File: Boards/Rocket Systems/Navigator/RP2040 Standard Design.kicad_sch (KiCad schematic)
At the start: 41 parts, among them J5 DX07S016JA1R1500, J6 BM03B-SRSS-TBLFSN, U7 W25Q128JVSIQ TR, U8 ST1L05APU33R

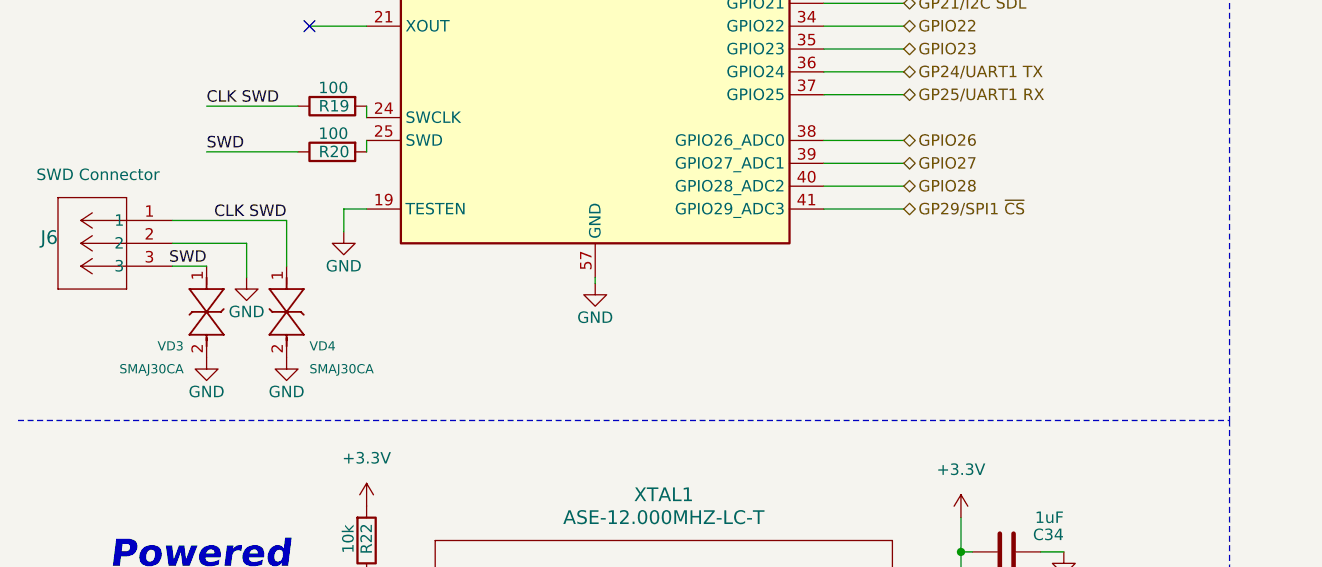
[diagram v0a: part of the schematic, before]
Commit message: ESD diodes and pinout update
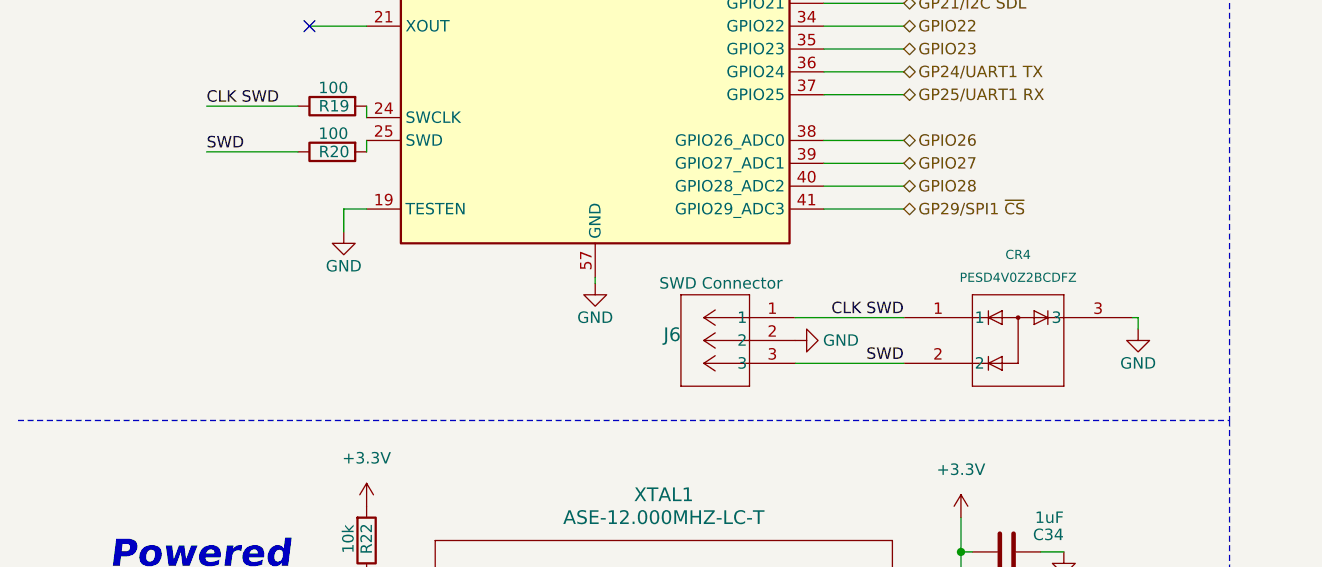
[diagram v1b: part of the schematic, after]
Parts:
- removed VD3, VD4: SMAJ30CA, SMAJ30CA:SMASeries_LTF, symbol SMAJ30CA:SMAJ30CA
- added CR4: PESD4V0Z2BCDFZ, DFN06033_SOT8013_NEX, symbol PESD4V0Z2BCDFZ:PESD4V0Z2BCDFZ
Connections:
- net CLK SWD: now also CR4.1
- net GND: now also CR4.3
- net SWD: now also CR4.2

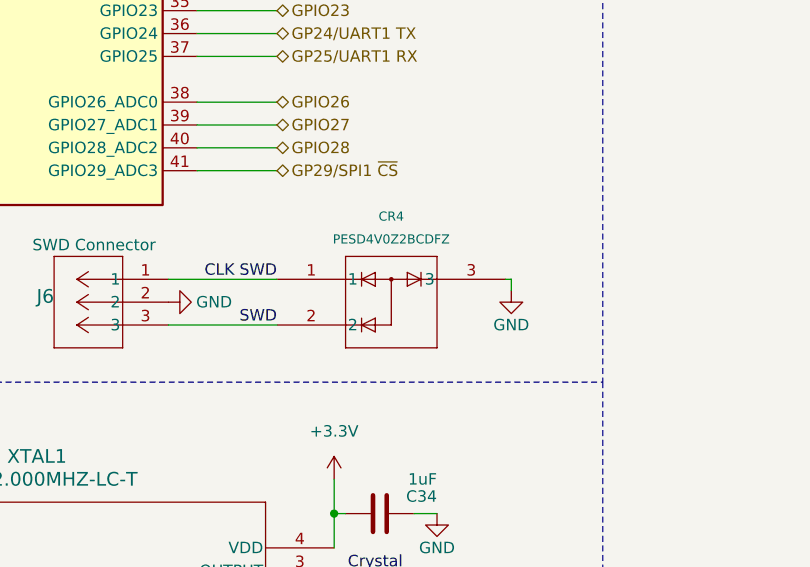
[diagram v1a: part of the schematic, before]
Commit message: ESD diode update
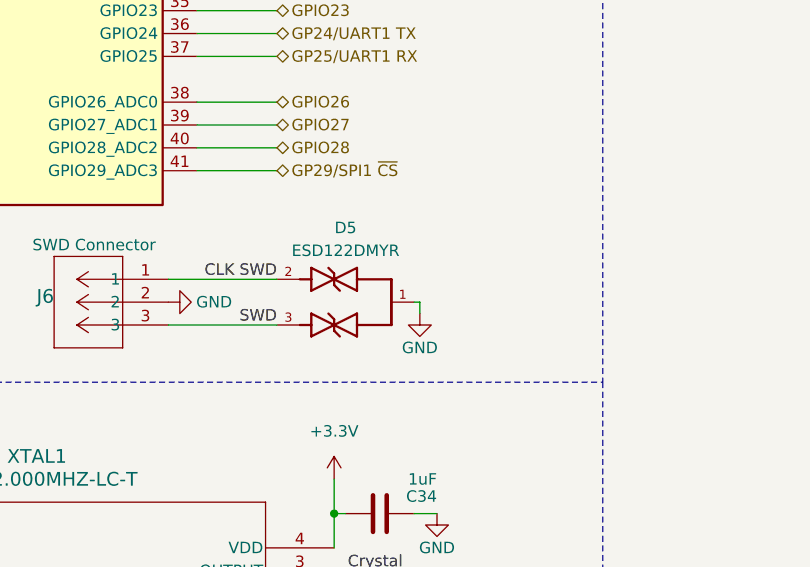
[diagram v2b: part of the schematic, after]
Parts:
- removed CR4: PESD4V0Z2BCDFZ, DFN06033_SOT8013_NEX, symbol PESD4V0Z2BCDFZ:PESD4V0Z2BCDFZ
- added D5: ESD122DMYR, 2Channel ESD HS-ESD122DMYR:DIO_ESD122DMYR, symbol ESD122DMYR:ESD122DMYR
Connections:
- net CLK SWD: now also D5.2
- net GND: now also D5.1
- net SWD: now also D5.3
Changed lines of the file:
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@@
 	(wire
 		(pts
+			(xy 125.73 156.845) (xy 126.365 156.845)
+		)
+		(stroke
+			(width 0)
+			(type default)
+		)
+	)
+	(wire
+		(pts
 			(xy 60.96 45.72) (xy 68.58 45.72)
 		)
@@
 	(wire
 		(pts
-			(xy 136.525 154.305) (xy 136.525 155.575)
+			(xy 126.365 156.845) (xy 126.365 158.115)
 		)
 		(stroke
@@
 	(wire
 		(pts
-			(xy 135.89 154.305) (xy 136.525 154.305)
-		)
-		(stroke
-			(width 0)
-			(type default)
-		)
-	)
-	(wire
-		(pts
 			(xy 71.12 58.42) (xy 73.66 58.42)
 		)
@@
 	(symbol
 		(lib_id "power:GND")
-		(at 136.525 155.575 0)
+		(at 126.365 158.115 0)
 		(unit 1)
 		(exclude_from_sim no)
@@
 		(dnp no)
 		(property "Reference" "#PWR087"
-			(at 136.525 161.925 0)
+			(at 126.365 164.465 0)
 			(effects
 				(font
@@
 		)
 		(property "Value" "GND"
-			(at 136.525 159.385 0)
+			(at 126.365 161.925 0)
 			(effects
 				(font
@@
 		)
 		(property "Footprint" ""
-			(at 136.525 155.575 0)
+			(at 126.365 158.115 0)
 			(effects
 				(font
@@
 		)
 		(property "Datasheet" ""
-			(at 136.525 155.575 0)
+			(at 126.365 158.115 0)
 			(effects
 				(font
@@
 		)
 		(property "Description" "Power symbol creates a global label with name \"GND\" , ground"
-			(at 136.525 155.575 0)
+			(at 126.365 158.115 0)
 			(effects
 				(font
@@
 	)
 	(symbol
+		(lib_id "ESD122DMYR:ESD122DMYR")
+		(at 118.11 156.845 0)
+		(unit 1)
+		(exclude_from_sim no)
+		(in_bom yes)
+		(on_board yes)
+		(dnp no)
+		(fields_autoplaced yes)
+		(property "Reference" "D5"
+			(at 118.11 148.59 0)
+			(effects
+				(font
+					(size 1.27 1.27)
+				)
+			)
+		)
+		(property "Value" "ESD122DMYR"
+			(at 118.11 151.13 0)
+			(effects
+				(font
+					(size 1.27 1.27)
+				)
+			)
+		)
+		(property "Footprint" "2Channel ESD HS-ESD122DMYR:DIO_ESD122DMYR"
+			(at 118.11 156.845 0)
+			(effects
+				(font
+					(size 1.27 1.27)
+				)
+				(justify bottom)
+				(hide yes)
+			)
+		)
+		(property "Datasheet" ""
+			(at 118.11 156.845 0)
+			(effects
+				(font
+					(size 1.27 1.27)
+				)
+				(hide yes)
+			)
+		)
+		(property "Description" ""
+			(at 118.11 156.845 0)
+			(effects
+				(font
+					(size 1.27 1.27)
+				)
+				(hide yes)
+			)
+		)
+		(property "MF" "Texas Instruments"
+			(at 118.11 156.845 0)
+			(effects
+				(font
+					(size 1.27 1.27)
+				)
+				(justify bottom)
+				(hide yes)
+			)
+		)
+		(property "SNAPEDA_PACKAGE_ID" "103746"
+			(at 118.11 156.845 0)
+			(effects
+				(font
+					(size 1.27 1.27)
+				)
+				(justify bottom)
+				(hide yes)
+			)
+		)
+		(property "Package" "X2SON-3 Texas Instruments"
+			(at 118.11 156.845 0)
+			(effects
+				(font
+					(size 1.27 1.27)
+				)
+				(justify bottom)
+				(hide yes)
+			)
+		)
+		(property "Price" "None"
+			(at 118.11 156.845 0)
+			(effects
+				(font
+					(size 1.27 1.27)
+				)
+				(justify bottom)
+				(hide yes)
+			)
+		)
+		(property "Check_prices" "https://www.snapeda.com/parts/ESD122DMYR/Texas+Instruments/view-part/?ref=eda"
+			(at 118.11 156.845 0)
+			(effects
+				(font
+					(size 1.27 1.27)
+				)
+				(justify bottom)
+				(hide yes)
+			)
+		)
+		(property "STANDARD" "Manufacturer Recommendations"
+			(at 118.11 156.845 0)
+			(effects
+				(font
+					(size 1.27 1.27)
+				)
+				(justify bottom)
+				(hide yes)
+			)
+		)
+		(property "PARTREV" "A"
+			(at 118.11 156.845 0)
+			(effects
+				(font
+					(size 1.27 1.27)
+				)
+				(justify bottom)
+				(hide yes)
+			)
+		)
+		(property "SnapEDA_Link" "https://www.snapeda.com/parts/ESD122DMYR/Texas+Instruments/view-part/?ref=snap"
+			(at 118.11 156.845 0)
+			(effects
+				(font
+					(size 1.27 1.27)
+				)
+				(justify bottom)
+				(hide yes)
+			)
+		)
+		(property "MP" "ESD122DMYR"
+			(at 118.11 156.845 0)
+			(effects
+				(font
+					(size 1.27 1.27)
+				)
+				(justify bottom)
+				(hide yes)
+			)
+		)
+		(property "Description_1" "Dual 0.2-pF, ±3.6-V, ±17-kV ESD protection diode for USB Type-C and HDMI 2.0"
+			(at 118.11 156.845 0)
+			(effects
+				(font
+					(size 1.27 1.27)
+				)
+				(justify bottom)
+				(hide yes)
+			)
+		)
+		(property "MANUFACTURER" "Texas Instruments"
+			(at 118.11 156.845 0)
+			(effects
+				(font
+					(size 1.27 1.27)
+				)
+				(justify bottom)
+				(hide yes)
+			)
+		)
+		(property "Availability" "In Stock"
+			(at 118.11 156.845 0)
+			(effects
+				(font
+					(size 1.27 1.27)
+				)
+				(justify bottom)
+				(hide yes)
+			)
+		)
+		(property "MAXIMUM_PACKAGE_HEIGHT" "0.4 mm"
+			(at 118.11 156.845 0)
+			(effects
+				(font
+					(size 1.27 1.27)
+				)
+				(justify bottom)
+				(hide yes)
+			)
+		)
+		(pin "3"
+		)
+		(pin "2"
+		)
+		(pin "1"
+		)
+		(instances
+			(project ""
+				(path "/1ff41ee6-31ba-481b-ae3a-c725064eb5fe/131a9704-942d-4843-a3d4-218a5885dac4"
+					(reference "D5")
+					(unit 1)
+				)
+			)
+		)
+	)
+	(symbol
 		(lib_id "power:+5V")
 		(at 211.455 151.13 0)
@@
 					(unit 1)
 				)
-			)
-		)
-	)
-	(symbol
-		(lib_id "PESD4V0Z2BCDFZ:PESD4V0Z2BCDFZ")
-		(at 110.49 154.305 0)
-		(unit 1)
-		(exclude_from_sim no)
-		(in_bom yes)
-		(on_board yes)
-		(dnp no)
-		(fields_autoplaced yes)
-		(property "Reference" "CR4"
-			(at 123.19 147.32 0)
-			(effects
-				(font
-					(size 1.016 1.016)
-				)
-			)
-		)
-		(property "Value" "PESD4V0Z2BCDFZ"
-			(at 123.19 149.86 0)
-			(effects
-				(font
-					(size 1.016 1.016)
-				)
-			)
-		)
-		(property "Footprint" "DFN06033_SOT8013_NEX"
-			(at 110.49 154.305 0)
-			(effects
-				(font
-					(size 1.27 1.27)
-					(italic yes)
-				)
-				(hide yes)
-			)
-		)
-		(property "Datasheet" "PESD4V0Z2BCDFZ"
-			(at 110.49 154.305 0)
-			(effects
-				(font
-					(size 1.27 1.27)
-					(italic yes)
-				)
-				(hide yes)
-			)
-		)
-		(property "Description" ""
-			(at 110.49 154.305 0)
-			(effects
-				(font
-					(size 1.27 1.27)
-				)
-				(hide yes)
-			)
-		)
-		(pin "2"
-		)
-		(pin "3"
-		)
-		(pin "1"
-		)
-		(instances
-			(project "Navigator"
-				(path "/1ff41ee6-31ba-481b-ae3a-c725064eb5fe/131a9704-942d-4843-a3d4-218a5885dac4"
-					(reference "CR4")
-					(unit 1)
-				)

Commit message: partial rounting done
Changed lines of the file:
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@@
 	(text "USB-C"
 		(exclude_from_sim no)
-		(at 149.86 117.475 0)
+		(at 262.128 118.11 0)
 		(effects
 			(font

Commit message: Nav & OBC update
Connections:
- net GP0/UART0 TX renamed GPIO0
- net GP18/SPI0 SCK renamed GP18/UART0 CTS
- net GP19/SPI0 MOSI renamed GP19/UART0 RTS
- net GP1/UART0 RX renamed GPIO1
- net GP24/UART1 TX renamed GPIO24
- net GP25/UART1 RX renamed GP25/SPI1 ~{CS}
- net GP29/SPI1 ~{CS} renamed GPIO29
- net GP2/UART0 CTS renamed GPIO2
- net GP3/UART0 RTS renamed GPIO3
- net GPIO16 renamed GP16/UART0 TX
- net GPIO17 renamed GP17/UART0 RX
- net GPIO4 renamed GP4/UART1 TX
- net GPIO5 renamed GP5/UART1 RX
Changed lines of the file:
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@@
 		)
 	)
-	(hierarchical_label "GP3{slash}UART0 RTS"
+	(hierarchical_label "GPIO3"
 		(shape bidirectional)
 		(at 110.49 73.66 0)
@@
 		)
 	)
-	(hierarchical_label "GP18{slash}SPI0 SCK"
+	(hierarchical_label "GP18{slash}UART0 CTS"
 		(shape bidirectional)
 		(at 110.49 111.76 0)
@@
 		)
 	)
-	(hierarchical_label "GP29{slash}SPI1 ~{CS}"
+	(hierarchical_label "GPIO29"
 		(shape bidirectional)
 		(at 110.49 142.24 0)
@@
 		)
 	)
-	(hierarchical_label "GP1{slash}UART0 RX"
+	(hierarchical_label "GPIO1"
 		(shape bidirectional)
 		(at 110.49 68.58 0)
@@
 		)
 	)
-	(hierarchical_label "GP25{slash}UART1 RX"
+	(hierarchical_label "GP25{slash}SPI1 ~{CS}"
 		(shape bidirectional)
 		(at 110.49 129.54 0)
@@
 		)
 	)
-	(hierarchical_label "GP19{slash}SPI0 MOSI"
+	(hierarchical_label "GP19{slash}UART0 RTS"
 		(shape bidirectional)
 		(at 110.49 114.3 0)
@@
 		)
 	)
-	(hierarchical_label "GPIO17"
+	(hierarchical_label "GP17{slash}UART0 RX"
 		(shape bidirectional)
 		(at 110.49 109.22 0)
@@
 		)
 	)
-	(hierarchical_label "GPIO4"
+	(hierarchical_label "GP4{slash}UART1 TX"
 		(shape bidirectional)
 		(at 110.49 76.2 0)
@@
 		)
 	)
-	(hierarchical_label "GPIO5"
+	(hierarchical_label "GP5{slash}UART1 RX"
 		(shape bidirectional)
 		(at 110.49 78.74 0)
@@
 		)
 	)
-	(hierarchical_label "GP2{slash}UART0 CTS"
+	(hierarchical_label "GPIO2"
 		(shape bidirectional)
 		(at 110.49 71.12 0)
@@
 		)
 	)
-	(hierarchical_label "GP0{slash}UART0 TX"
+	(hierarchical_label "GPIO0"
 		(shape bidirectional)
 		(at 110.49 66.04 0)
@@
 		)
 	)
-	(hierarchical_label "GP24{slash}UART1 TX"
+	(hierarchical_label "GPIO24"
 		(shape bidirectional)
 		(at 110.49 127 0)
@@
 		)
 	)
-	(hierarchical_label "GPIO16"
+	(hierarchical_label "GP16{slash}UART0 TX"
 		(shape bidirectional)
 		(at 110.49 106.68 0)

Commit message: PocketSat Finished
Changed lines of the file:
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@@
 	(text "USB-C"
 		(exclude_from_sim no)
-		(at 262.128 118.11 0)
+		(at 150.495 119.38 0)
 		(effects
 			(font

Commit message: Nav Update
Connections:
- net GND: now also J6.4 (EP), J6.5 (EP)
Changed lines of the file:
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@@
+	)
+	(symbol
+		(lib_id "power:GND")
+		(at 97.155 161.925 90)
+		(unit 1)
+		(exclude_from_sim no)
+		(in_bom yes)
+		(on_board yes)
+		(dnp no)
+		(property "Reference" "#PWR058"
+			(at 103.505 161.925 0)
+			(effects
+				(font
+					(size 1.27 1.27)
+				)
+				(hide yes)
+			)
+		)
+		(property "Value" "GND"
+			(at 102.235 161.925 90)
+			(effects
+				(font
+					(size 1.27 1.27)
+				)
+			)
+		)
+		(property "Footprint" ""
+			(at 97.155 161.925 0)
+			(effects
+				(font
+					(size 1.27 1.27)
+				)
+				(hide yes)
+			)
+		)
+		(property "Datasheet" ""
+			(at 97.155 161.925 0)
+			(effects
+				(font
+					(size 1.27 1.27)
+				)
+				(hide yes)
+			)
+		)
+		(property "Description" "Power symbol creates a global label with name \"GND\" , ground"
+			(at 97.155 161.925 0)
+			(effects
+				(font
+					(size 1.27 1.27)
+				)
+				(hide yes)
+			)
+		)
+		(pin "1"
+		)
+		(instances
+			(project "Navigator"
+				(path "/1ff41ee6-31ba-481b-ae3a-c725064eb5fe/131a9704-942d-4843-a3d4-218a5885dac4"
+					(reference "#PWR058")
+					(unit 1)
+				)
+			)
+		)
 	)
 	(symbol
@@
 		(pin "2"
 		)
-		(instances
+		(pin "4"
+		)
+		(pin "5"
+		)
+		(instances

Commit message: DFM checks, Avionics Updates
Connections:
- net GPIO29 renamed GP29/ADC3
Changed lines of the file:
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@@
 		)
 	)
-	(hierarchical_label "GPIO29"
+	(hierarchical_label "GP29{slash}ADC3"
 		(shape bidirectional)
 		(at 110.49 142.24 0)
